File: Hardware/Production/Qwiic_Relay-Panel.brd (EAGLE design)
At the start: 84.1 x 109 mm, 198 parts, among them J11 Qwiic Right Angle, J12 Qwiic Right Angle, J13 AVR_SPI_PROG_3X2TESTPOINTS, J16 Qwiic Right Angle, J17 Qwiic Right Angle, J18 AVR_SPI_PROG_3X2TESTPOINTS, J2 Qwiic Right Angle, J21 Qwiic Right Angle, J22 Qwiic Right Angle, J23 AVR_SPI_PROG_3X2TESTPOINTS, J26 Qwiic Right Angle, J27 Qwiic Right Angle, J28 AVR_SPI_PROG_3X2TESTPOINTS, J3 Qwiic Right Angle, J4 AVR_SPI_PROG_3X2TESTPOINTS, J6 Qwiic Right Angle, J7 Qwiic Right Angle, J8 AVR_SPI_PROG_3X2TESTPOINTS, Q1 600mA/40V, Q2 600mA/40V, Q3 600mA/40V, Q4 600mA/40V, Q5 600mA/40V, Q6 600mA/40V, U1 ATTIN85_SOIC_5.3MM, U10 OPTO_ISOLATOR_DIP, U11 ATTIN85_SOIC_5.3MM, U12 OPTO_ISOLATOR_DIP, U2 OPTO_ISOLATOR_DIP, U3 ATTIN85_SOIC_5.3MM, U4 OPTO_ISOLATOR_DIP, U5 ATTIN85_SOIC_5.3MM, U6 OPTO_ISOLATOR_DIP, U7 ATTIN85_SOIC_5.3MM, U8 OPTO_ISOLATOR_DIP, U9 ATTIN85_SOIC_5.3MM

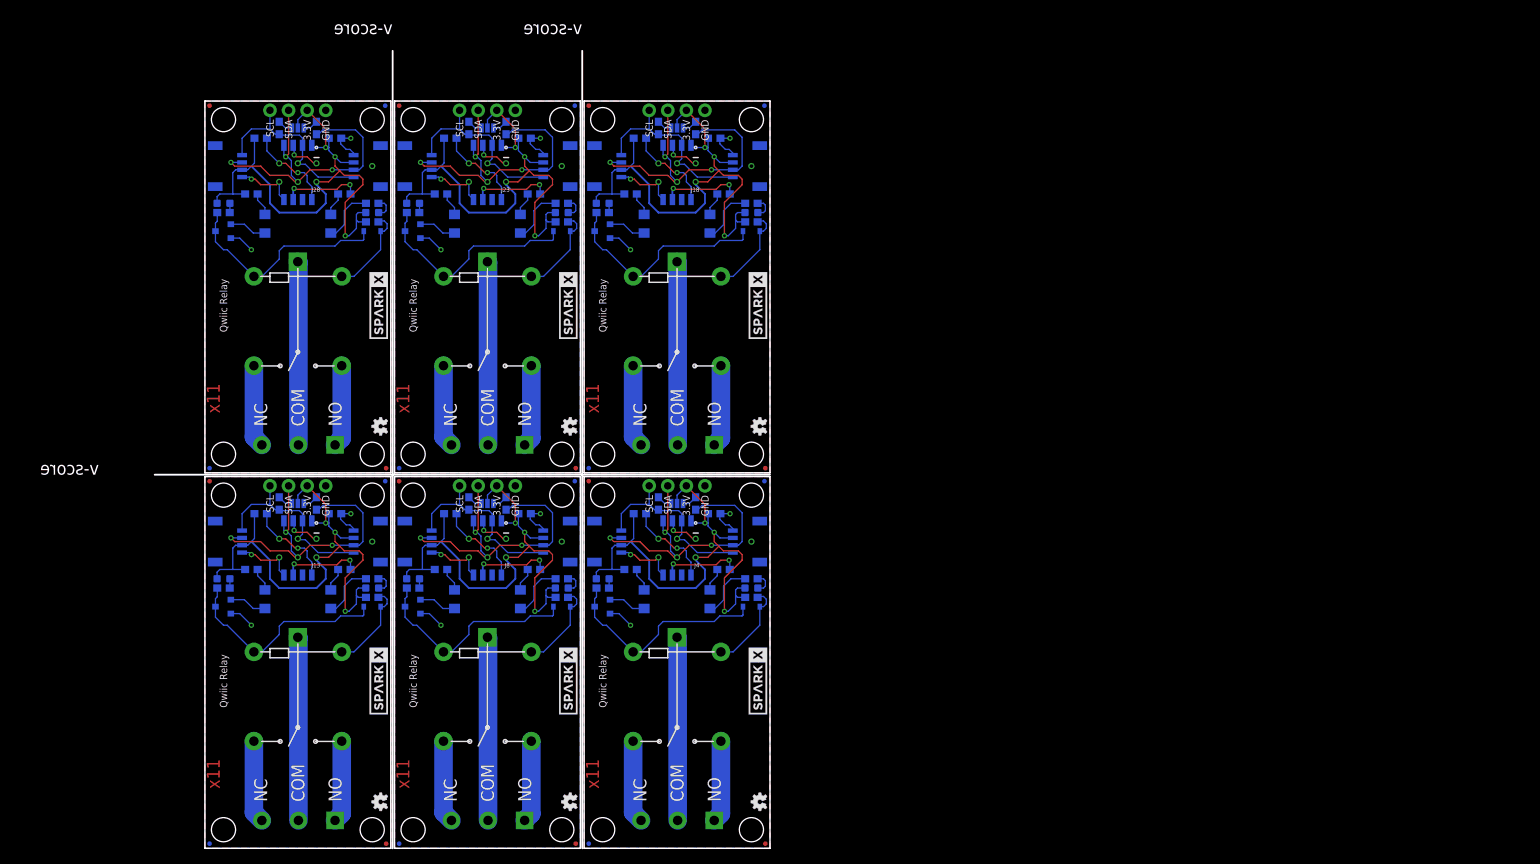
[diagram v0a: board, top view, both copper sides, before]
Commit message: added Example 1- Basic Control and Example 2- Change Address
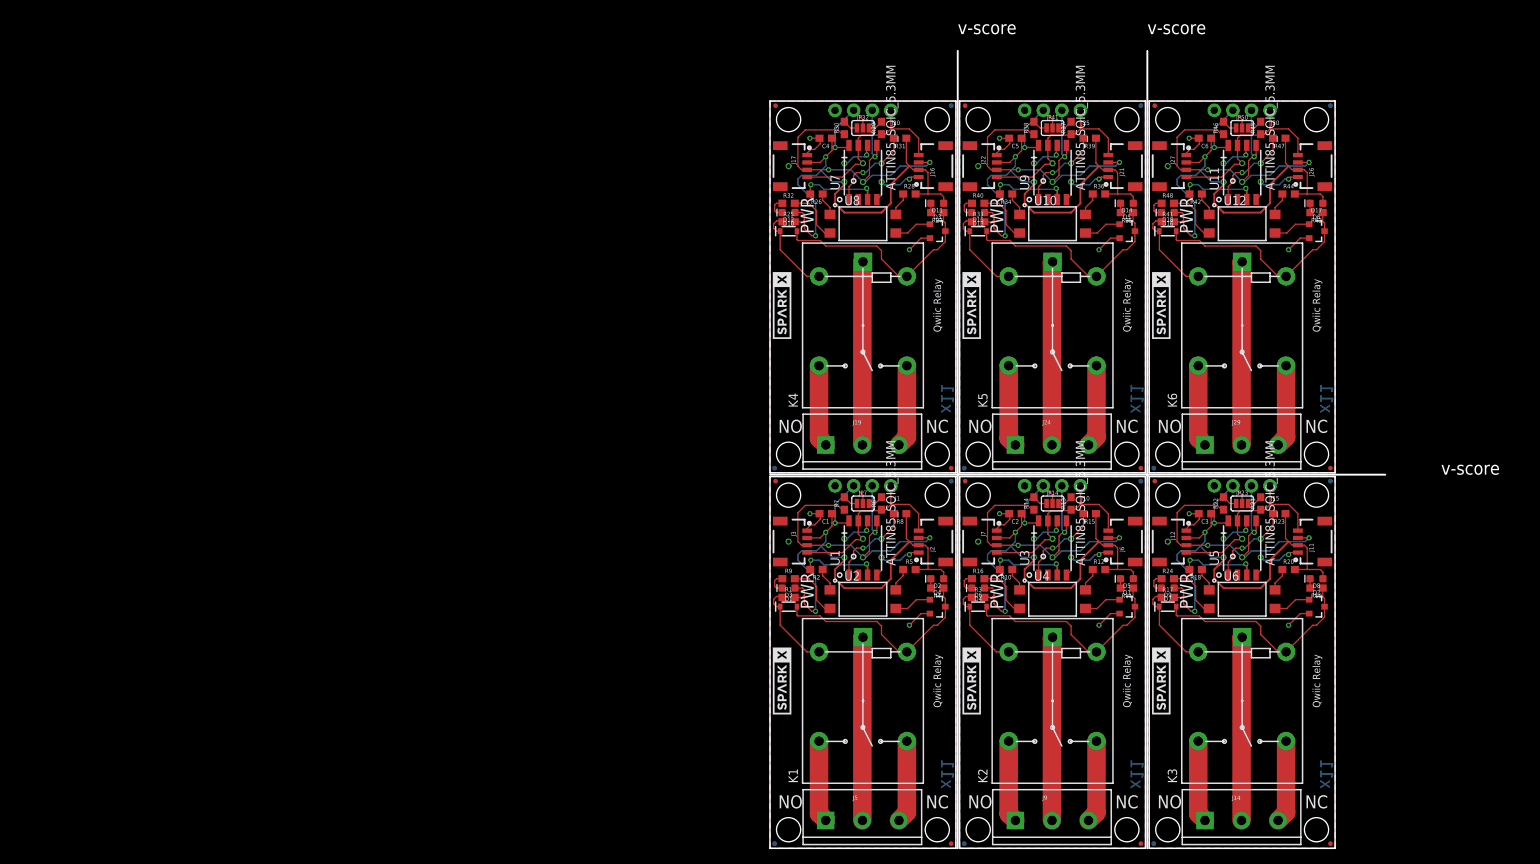
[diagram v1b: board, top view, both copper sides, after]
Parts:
- moved JP21 153.2 mm to (76.6, 50.2), flipped to the bottom
- moved JP26 153.2 mm to (76.6, 0.64), flipped to the top
- moved JP48 153.2 mm to (76.6, 101.5), flipped to the bottom
- moved JP53 153.2 mm to (76.6, 51.9), flipped to the top
- moved D17 149.4 mm to (74.7, 88.1), flipped to the top
- moved D8 149.4 mm to (74.7, 36.8), flipped to the top
- moved JP20 149.4 mm to (74.7, 48.3), flipped to the top
- moved JP25 149.4 mm to (74.7, 2.54), flipped to the top
- moved JP47 149.4 mm to (74.7, 99.6), flipped to the top
- moved JP52 149.4 mm to (74.7, 53.8), flipped to the top
- moved Q2 149.4 mm to (74.7, 33.0), flipped to the top
- moved Q6 149.4 mm to (74.7, 84.3), flipped to the top
- moved R19 149.4 mm to (74.7, 35.6), flipped to the top
- moved R43 149.4 mm to (74.7, 86.9), flipped to the top
- moved J11 144.3 mm to (72.1, 41.9), flipped to the top
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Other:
- outline, holes or cut-outs redrawn
